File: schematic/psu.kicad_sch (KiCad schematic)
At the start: 19 parts, among them J0 Conn_01x04

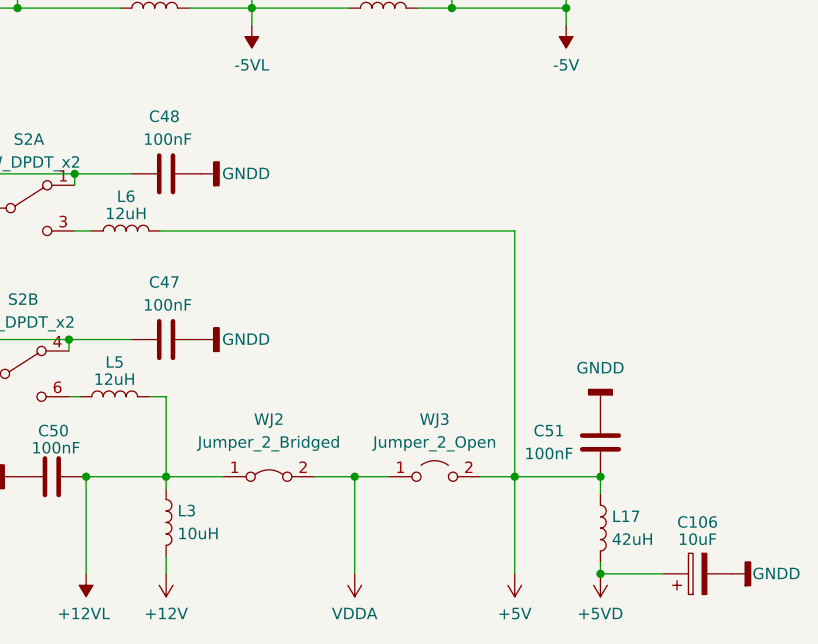
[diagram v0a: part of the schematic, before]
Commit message: first draft of board with components added, no traces
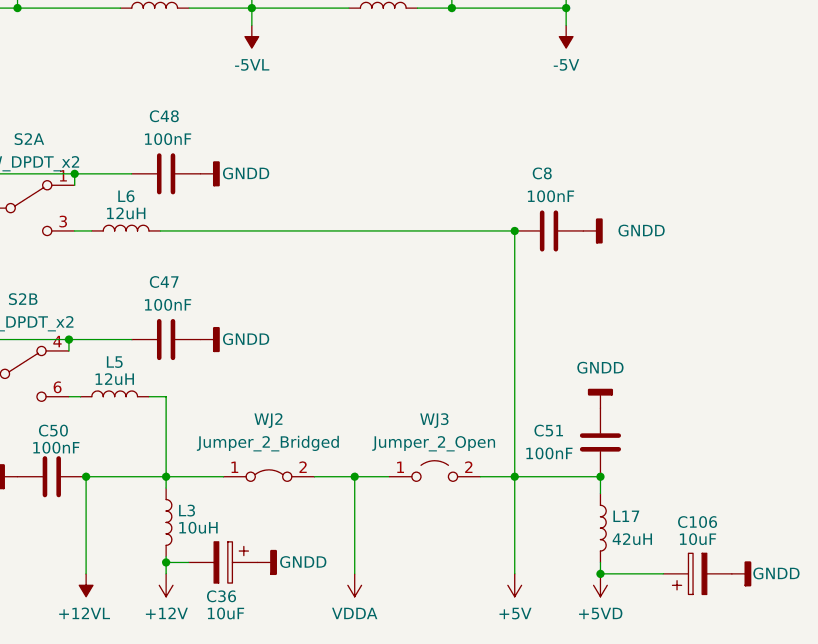
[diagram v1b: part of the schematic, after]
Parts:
- added C36: 10uF, Capacitor_THT:CP_Radial_D5.0mm_P2.50mm, symbol Device:C_Polarized
- added C8: 100nF, Capacitor_THT:C_Disc_D7.0mm_W2.5mm_P5.00mm, symbol Device:C
- C106, C34: footprint Capacitor_THT:CP_Radial_D5.0mm_P2.00mm -> Capacitor_THT:CP_Radial_D5.0mm_P2.50mm
- C41, C46, C47, C48, C49, C50, C51: footprint Capacitor_THT:C_Disc_D10.0mm_W2.5mm_P5.00mm -> Capacitor_THT:C_Disc_D7.0mm_W2.5mm_P5.00mm
- L17, L2, L3, L4: footprint Inductor_THT:L_Axial_L12.8mm_D5.8mm_P7.62mm_Vertical_Fastron_HBCC -> Inductor_THT:L_Axial_L11.0mm_D4.5mm_P7.62mm_Vertical_Fastron_MECC
- L5, L6: footprint Inductor_THT:L_Axial_L12.0mm_D5.0mm_P15.24mm_Horizontal_Fastron_MISC -> Inductor_THT:L_Axial_L12.8mm_D5.8mm_P25.40mm_Horizontal_Fastron_HBCC
- S2: footprint Button_Switch_THT:SW_E-Switch_EG1271_SPDT -> Switches_THT:DPDT_GF-626-0061
- WJ2, WJ3: footprint Resistor_THT:R_Axial_DIN0204_L3.6mm_D1.6mm_P7.62mm_Horizontal -> Resistor_THT:R_Axial_DIN0207_L6.3mm_D2.5mm_P15.24mm_Horizontal
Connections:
- net +12V: now also C36.2
- net +5V: now also C8.2
- net GNDD: now also C36.1, C8.1

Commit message: RF on main board components setup correctly.
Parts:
- C106: footprint Capacitor_THT:CP_Radial_D5.0mm_P2.50mm -> Capacitor_THT:CP_Radial_Tantal_D4.5mm_P2.50mm
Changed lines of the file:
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@@
     (property "Reference" "C106" (id 0) (at 214.63 132.08 90))
     (property "Value" "10uF" (id 1) (at 214.63 133.985 90))
-    (property "Footprint" "Capacitor_THT:CP_Radial_D5.0mm_P2.50mm" (id 2) (at 218.44 136.8298 0)
+    (property "Footprint" "Capacitor_THT:CP_Radial_Tantal_D4.5mm_P2.50mm" (id 2) (at 218.44 136.8298 0)
       (effects (font (size 1.27 1.27)) hide)
     )

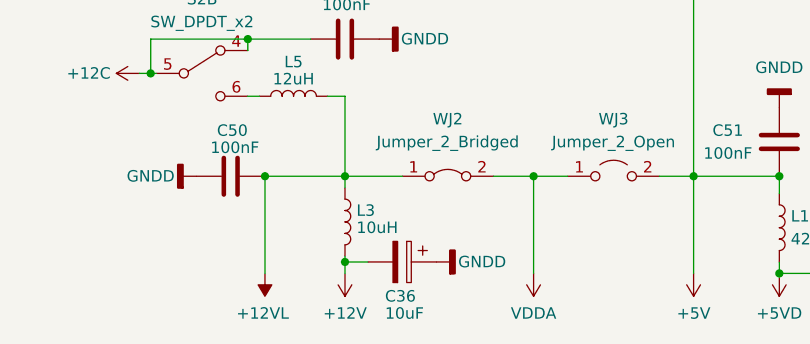
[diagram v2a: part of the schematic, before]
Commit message: added traces to parts of the clock gen/reset ic's
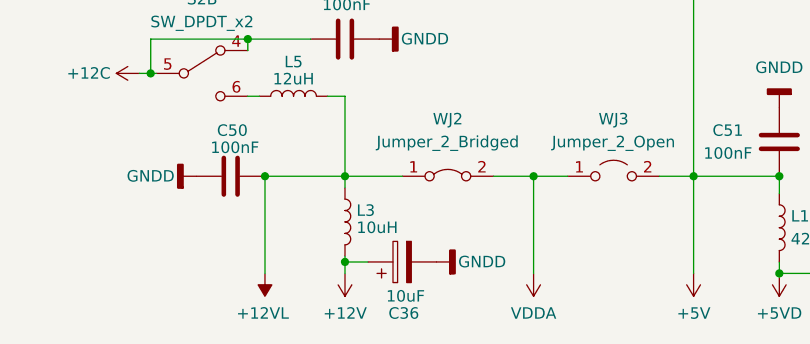
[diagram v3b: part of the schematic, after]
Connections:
- net +12V: now also C36.1; no longer C36.2
- net GNDD: now also C36.2; no longer C36.1
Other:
- moved on the sheet: C36
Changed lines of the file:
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@@
     (pin "1")
   )
-  (symbol (lib_id "Device:C_Polarized") (at 161.925 136.525 270) (unit 1)
+  (symbol (lib_id "Device:C_Polarized") (at 161.925 136.525 90) (unit 1)
     (in_bom yes) (on_board yes)
-    (property "Reference" "C36" (id 0) (at 160.02 140.335 90)
+    (property "Reference" "C36" (id 0) (at 163.83 142.24 90)
       (effects (font (size 1.27 1.27)) (justify left))
     )
-    (property "Value" "10uF" (id 1) (at 160.02 142.24 90)
+    (property "Value" "10uF" (id 1) (at 164.465 140.335 90)
       (effects (font (size 1.27 1.27)) (justify left))
     )
-    (property "Footprint" "Capacitor_THT:CP_Radial_D5.0mm_P2.50mm" (id 2) (at 158.115 137.4902 0)
+    (property "Footprint" "Capacitor_THT:CP_Radial_D5.0mm_P2.50mm" (id 2) (at 165.735 135.5598 0)
       (effects (font (size 1.27 1.27)) hide)
     )

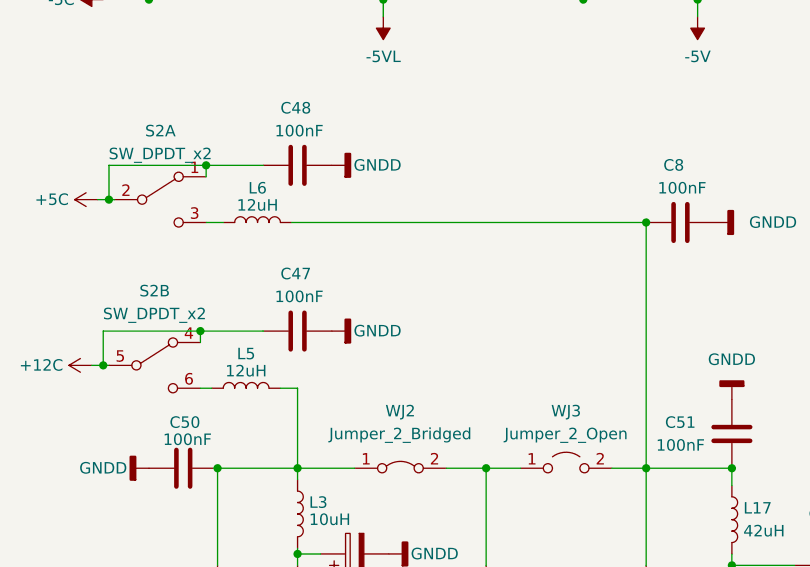
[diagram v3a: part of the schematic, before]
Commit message: fixed a bug on the +5v line, added +5NF (no filter) net list names. Added traces to the ram, and inverter, and select ics.
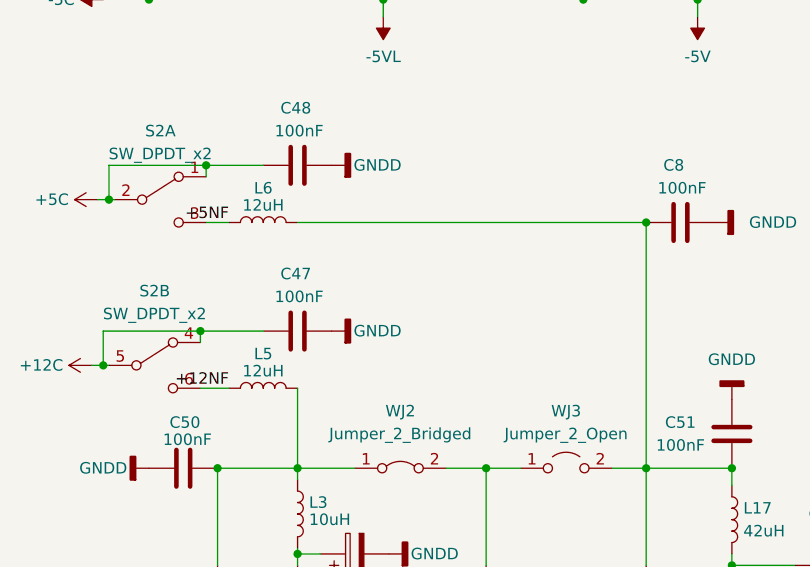
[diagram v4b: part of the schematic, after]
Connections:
- net +5NF: now reaches L6.1, S2.3 (C)
- net +12NF: now reaches L5.1, S2.6 (C)
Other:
- moved on the sheet: L5, L6
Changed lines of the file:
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@@
     (stroke (width 0) (type default) (color 0 0 0 0))
   )
-  (wire (pts (xy 154.94 99.695) (xy 194.31 99.695))
-    (stroke (width 0) (type default) (color 0 0 0 0))
-  )
-  (wire (pts (xy 153.67 118.11) (xy 155.575 118.11))
+  (wire (pts (xy 155.575 99.695) (xy 194.31 99.695))
     (stroke (width 0) (type default) (color 0 0 0 0))
   )
@@
     (stroke (width 0) (type default) (color 0 0 0 0))
   )
-  (wire (pts (xy 144.78 118.11) (xy 146.05 118.11))
+  (wire (pts (xy 144.78 118.11) (xy 147.955 118.11))
     (stroke (width 0) (type default) (color 0 0 0 0))
   )
@@
     (stroke (width 0) (type default) (color 0 0 0 0))
   )
-  (wire (pts (xy 145.415 99.695) (xy 147.32 99.695))
+  (wire (pts (xy 145.415 99.695) (xy 147.955 99.695))
     (stroke (width 0) (type default) (color 0 0 0 0))
   )
@@
     (effects (font (size 1.27 1.27)) (justify left bottom))
   )
-  (symbol (lib_id "Device:L") (at 151.13 99.695 90) (unit 1)
-    (in_bom yes) (on_board yes)
-    (property "Reference" "L6" (id 0) (at 151.13 95.885 90))
-    (property "Value" "12uH" (id 1) (at 151.13 97.79 90))
-    (property "Footprint" "Inductor_THT:L_Axial_L12.8mm_D5.8mm_P25.40mm_Horizontal_Fastron_HBCC" (id 2) (at 151.13 99.695 0)
-      (effects (font (size 1.27 1.27)) hide)
-    )
-    (property "Datasheet" "~" (id 3) (at 151.13 99.695 0)
+  (label "+12NF" (at 147.955 118.11 180)
+    (effects (font (size 1.27 1.27)) (justify right bottom))
+  )
+  (label "+5NF" (at 147.955 99.695 180)
+    (effects (font (size 1.27 1.27)) (justify right bottom))
+  )
+  (symbol (lib_id "Device:L") (at 151.765 99.695 90) (unit 1)
+    (in_bom yes) (on_board yes)
+    (property "Reference" "L6" (id 0) (at 151.765 95.885 90))
+    (property "Value" "12uH" (id 1) (at 151.765 97.79 90))
+    (property "Footprint" "Inductor_THT:L_Axial_L12.8mm_D5.8mm_P25.40mm_Horizontal_Fastron_HBCC" (id 2) (at 151.765 99.695 0)
+      (effects (font (size 1.27 1.27)) hide)
+    )
+    (property "Datasheet" "~" (id 3) (at 151.765 99.695 0)
       (effects (font (size 1.27 1.27)) hide)
     )
@@
     (pin "2")
   )
-  (symbol (lib_id "Device:L") (at 149.86 118.11 90) (unit 1)
-    (in_bom yes) (on_board yes)
-    (property "Reference" "L5" (id 0) (at 149.86 114.3 90))
-    (property "Value" "12uH" (id 1) (at 149.86 116.205 90))
-    (property "Footprint" "Inductor_THT:L_Axial_L12.8mm_D5.8mm_P25.40mm_Horizontal_Fastron_HBCC" (id 2) (at 149.86 118.11 0)
-      (effects (font (size 1.27 1.27)) hide)
-    )
-    (property "Datasheet" "~" (id 3) (at 149.86 118.11 0)
-      (effects (font (size 1.27 1.27)) hide)
-    )
+  (symbol (lib_id "Device:L") (at 151.765 118.11 90) (unit 1)
+    (in_bom yes) (on_board yes)
+    (property "Reference" "L5" (id 0) (at 151.765 114.3 90))
+    (property "Value" "12uH" (id 1) (at 151.765 116.205 90))
+    (property "Footprint" "Inductor_THT:L_Axial_L12.8mm_D5.8mm_P25.40mm_Horizontal_Fastron_HBCC" (id 2) (at 151.765 118.11 0)
+      (effects (font (size 1.27 1.27)) hide)
+    )
+    (property "Datasheet" "~" (id 3) (at 151.765 118.11 0)
+      (effects (font (size 1.27 1.27)) hide)
+    )

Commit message: added memory, eprom and sound lines. some video as well. fixed the cap size for polar. its a bit weird since they use 5 mm pin and 5mm body and bend out the leads.
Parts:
- C34, C36: footprint Capacitor_THT:CP_Radial_D5.0mm_P2.50mm -> Capacitor_THT:CP_Radial_Tantal_D4.5mm_P5.00mm
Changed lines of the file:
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@@
       (effects (font (size 1.27 1.27)) (justify left))
     )
-    (property "Footprint" "Capacitor_THT:CP_Radial_D5.0mm_P2.50mm" (id 2) (at 188.2902 73.025 0)
+    (property "Footprint" "Capacitor_THT:CP_Radial_Tantal_D4.5mm_P5.00mm" (id 2) (at 188.2902 73.025 0)
       (effects (font (size 1.27 1.27)) hide)
     )
@@
       (effects (font (size 1.27 1.27)) (justify left))
     )
-    (property "Footprint" "Capacitor_THT:CP_Radial_D5.0mm_P2.50mm" (id 2) (at 165.735 135.5598 0)
-      (effects (font (size 1.27 1.27)) hide)
-    )
+    (property "Footprint" "Capacitor_THT:CP_Radial_Tantal_D4.5mm_P5.00mm" (id 2) (at 165.735 135.5598 0)
+      (effects (font (size 1.27 1.27)) hide)
+    )

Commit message: added new models, fixed the drc errors. changed power width.
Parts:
- C34, C36: footprint Capacitor_THT:CP_Radial_Tantal_D4.5mm_P5.00mm -> Capacitor_THT:CP_Radial_D8.0mm_P5.00mm
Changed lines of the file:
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@@
       (effects (font (size 1.27 1.27)) (justify left))
     )
-    (property "Footprint" "Capacitor_THT:CP_Radial_Tantal_D4.5mm_P5.00mm" (id 2) (at 188.2902 73.025 0)
+    (property "Footprint" "Capacitor_THT:CP_Radial_D8.0mm_P5.00mm" (id 2) (at 188.2902 73.025 0)
       (effects (font (size 1.27 1.27)) hide)
     )
@@
       (effects (font (size 1.27 1.27)) (justify left))
     )
-    (property "Footprint" "Capacitor_THT:CP_Radial_Tantal_D4.5mm_P5.00mm" (id 2) (at 165.735 135.5598 0)
-      (effects (font (size 1.27 1.27)) hide)
-    )
+    (property "Footprint" "Capacitor_THT:CP_Radial_D8.0mm_P5.00mm" (id 2) (at 165.735 135.5598 0)
+      (effects (font (size 1.27 1.27)) hide)
+    )

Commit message: updated schematic with new layout
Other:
- company: (none) -> sparkletron
- title: Colecovision Schematic -> Reverse Engineer Colecovision
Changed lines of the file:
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@@
   (paper "USLetter")
   (title_block
-    (title "Colecovision Schematic")
-    (date "2023-01-09")
-    (rev "F.0")
+    (title "Reverse Engineer Colecovision")
+    (date "2023-03-14")
+    (rev "DEV")
+    (company "sparkletron")
     (comment 1 "Jay Convertino")
+    (comment 2 "MIT LICENSE")
   )
   (junction (at 194.31 99.695) (diameter 0) (color 0 0 0 0)

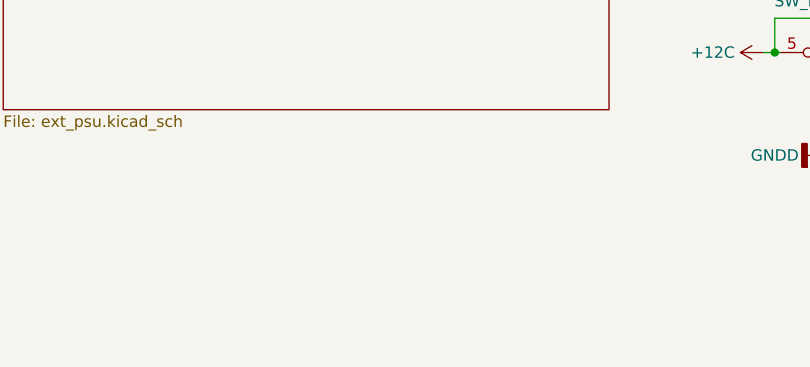
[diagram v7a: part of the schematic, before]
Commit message: added pads for switch and RF shield, RF shield still needs adjustment
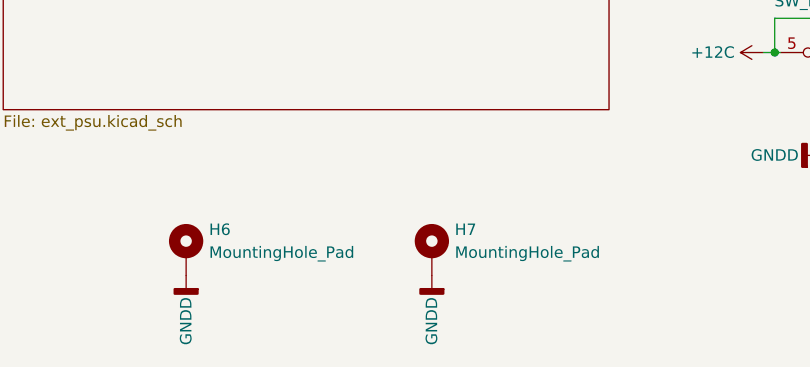
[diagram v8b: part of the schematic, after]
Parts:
- added H6, H7: MountingHole_Pad, mount_points:SWITCH_MOUNT, symbol Mechanical:MountingHole_Pad
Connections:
- net GNDD: now also H6.1, H7.1
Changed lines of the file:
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@@
     (pin "2")
+  )
+  (symbol (lib_id "power:GNDD") (at 68.58 140.335 0) (mirror y) (unit 1)
+    (in_bom yes) (on_board yes)
+    (property "Reference" "#PWR0252" (id 0) (at 68.58 146.685 0)
+      (effects (font (size 1.27 1.27)) hide)
+    )
+    (property "Value" "GNDD" (id 1) (at 68.58 145.415 90))
+    (property "Footprint" "" (id 2) (at 68.58 140.335 0)
+      (effects (font (size 1.27 1.27)) hide)
+    )
+    (property "Datasheet" "" (id 3) (at 68.58 140.335 0)
+      (effects (font (size 1.27 1.27)) hide)
+    )
+    (pin "1")
   )
   (symbol (lib_id "Device:C") (at 165.1 69.215 0) (unit 1)
@@
     )
     (property "Datasheet" "" (id 3) (at 133.985 74.93 0)
+      (effects (font (size 1.27 1.27)) hide)
+    )
+    (pin "1")
+  )
+  (symbol (lib_id "power:GNDD") (at 95.885 140.335 0) (mirror y) (unit 1)
+    (in_bom yes) (on_board yes)
+    (property "Reference" "#PWR0251" (id 0) (at 95.885 146.685 0)
+      (effects (font (size 1.27 1.27)) hide)
+    )
+    (property "Value" "GNDD" (id 1) (at 95.885 145.415 90))
+    (property "Footprint" "" (id 2) (at 95.885 140.335 0)
+      (effects (font (size 1.27 1.27)) hide)
+    )
+    (property "Datasheet" "" (id 3) (at 95.885 140.335 0)
       (effects (font (size 1.27 1.27)) hide)
     )
@@
     (pin "1")
   )
+  (symbol (lib_id "Mechanical:MountingHole_Pad") (at 95.885 137.795 0) (unit 1)
+    (in_bom yes) (on_board yes) (fields_autoplaced)
+    (property "Reference" "H7" (id 0) (at 98.425 135.2549 0)
+      (effects (font (size 1.27 1.27)) (justify left))
+    )
+    (property "Value" "MountingHole_Pad" (id 1) (at 98.425 137.7949 0)
+      (effects (font (size 1.27 1.27)) (justify left))
+    )
+    (property "Footprint" "mount_points:SWITCH_MOUNT" (id 2) (at 95.885 137.795 0)
+      (effects (font (size 1.27 1.27)) hide)
+    )
+    (property "Datasheet" "~" (id 3) (at 95.885 137.795 0)
+      (effects (font (size 1.27 1.27)) hide)
+    )
+    (pin "1")
+  )
   (symbol (lib_id "Device:L") (at 203.835 132.715 0) (unit 1)
     (in_bom yes) (on_board yes) (fields_autoplaced)
@@
     (pin "2")
   )
+  (symbol (lib_id "Mechanical:MountingHole_Pad") (at 68.58 137.795 0) (unit 1)
+    (in_bom yes) (on_board yes) (fields_autoplaced)
+    (property "Reference" "H6" (id 0) (at 71.12 135.2549 0)
+      (effects (font (size 1.27 1.27)) (justify left))
+    )
+    (property "Value" "MountingHole_Pad" (id 1) (at 71.12 137.7949 0)
+      (effects (font (size 1.27 1.27)) (justify left))
+    )
+    (property "Footprint" "mount_points:SWITCH_MOUNT" (id 2) (at 68.58 137.795 0)
+      (effects (font (size 1.27 1.27)) hide)
+    )
+    (property "Datasheet" "~" (id 3) (at 68.58 137.795 0)
+      (effects (font (size 1.27 1.27)) hide)
+    )
+    (pin "1")
+  )
   (symbol (lib_id "Device:L") (at 151.765 118.11 90) (unit 1)
